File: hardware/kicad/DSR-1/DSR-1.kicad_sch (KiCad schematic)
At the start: 0 parts

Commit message: Refactor code structure for improved readability and maintainability
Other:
- sheet Power input zone ports: added none; removed 9V_PD, B+1_RAW
- sheet Power management ports: added none; removed 9V_PD, B+1_RAW
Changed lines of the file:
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@@
-	(wire
-		(pts
-			(xy 120.65 39.37) (xy 153.67 39.37)
-		)
-		(stroke
-			(width 0)
-			(type default)
-		)
-	)
 	(wire
 		(pts
@@
 	(wire
 		(pts
-			(xy 120.65 43.18) (xy 151.13 43.18)
-		)
-		(stroke
-			(width 0)
-			(type default)
-		)
-	)
-	(wire
-		(pts
-			(xy 153.67 45.72) (xy 163.83 45.72)
-		)
-		(stroke
-			(width 0)
-			(type default)
-		)
-	)
-	(wire
-		(pts
-			(xy 151.13 43.18) (xy 151.13 55.88)
-		)
-		(stroke
-			(width 0)
-			(type default)
-		)
-	)
-	(wire
-		(pts
 			(xy 359.41 22.86) (xy 128.27 22.86)
 		)
@@
 	(wire
 		(pts
-			(xy 151.13 55.88) (xy 163.83 55.88)
-		)
-		(stroke
-			(width 0)
-			(type default)
-		)
-	)
-	(wire
-		(pts
 			(xy 77.47 138.43) (xy 86.36 138.43)
 		)
@@
 		(pts
 			(xy 128.27 22.86) (xy 128.27 54.61)
-		)
-		(stroke
-			(width 0)
-			(type default)
-		)
-	)
-	(wire
-		(pts
-			(xy 153.67 39.37) (xy 153.67 45.72)
 		)
 		(stroke
@@
 			)
 		)
-		(pin "9V_PD" output
-			(at 120.65 39.37 0)
-			(effects
-				(font
-					(size 1.27 1.27)
-				)
-				(justify right)
-			)
-		)
-		(pin "B+1_RAW" output
-			(at 120.65 43.18 0)
-			(effects
-				(font
-					(size 1.27 1.27)
-				)
-				(justify right)
-			)
-		)
 		(pin "CC1" bidirectional
 			(at 120.65 50.8 0)
@@
 			)
 		)
-		(pin "9V_PD" input
-			(at 163.83 45.72 180)
-			(effects
-				(font
-					(size 1.27 1.27)
-				)
-				(justify left)
-			)
-		)
-		(pin "B+1_RAW" input
-			(at 163.83 55.88 180)
-			(effects
-				(font
-					(size 1.27 1.27)
-				)
-				(justify left)
-			)
-		)

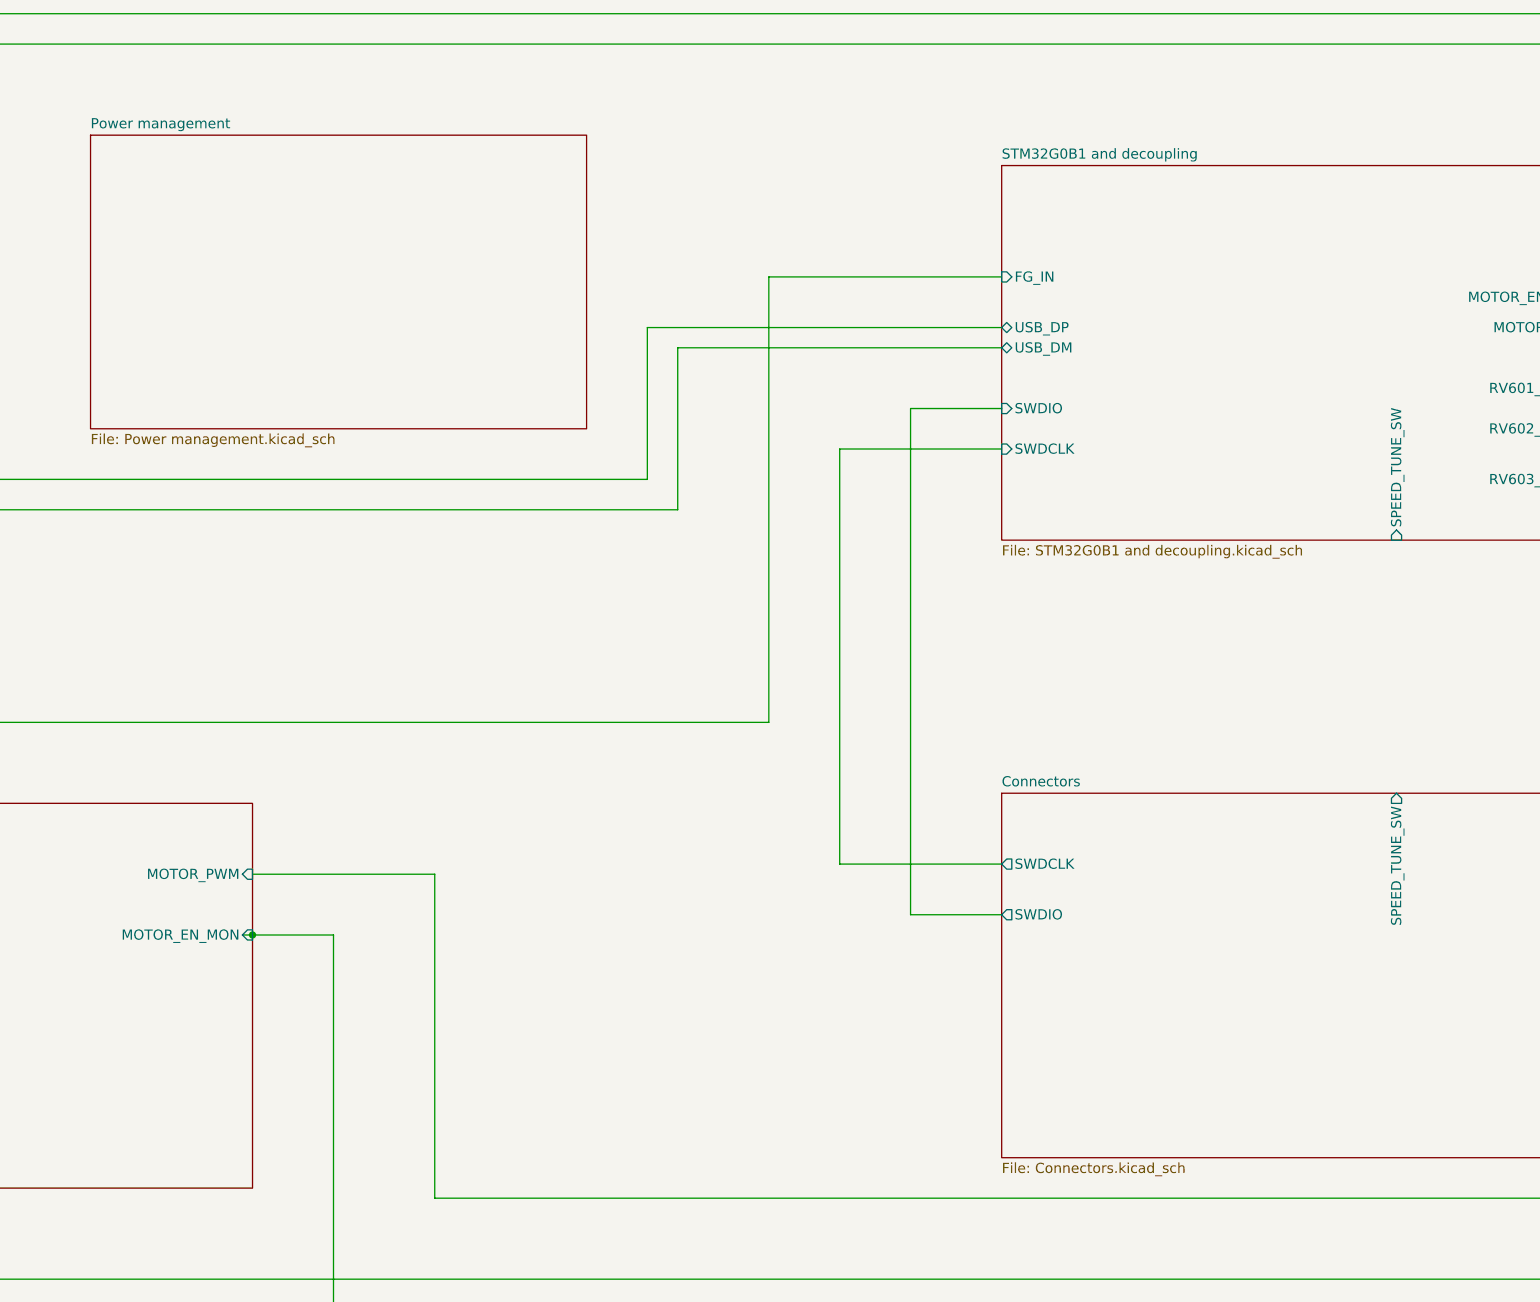
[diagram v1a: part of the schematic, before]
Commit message: completed schematics through sheet 5.
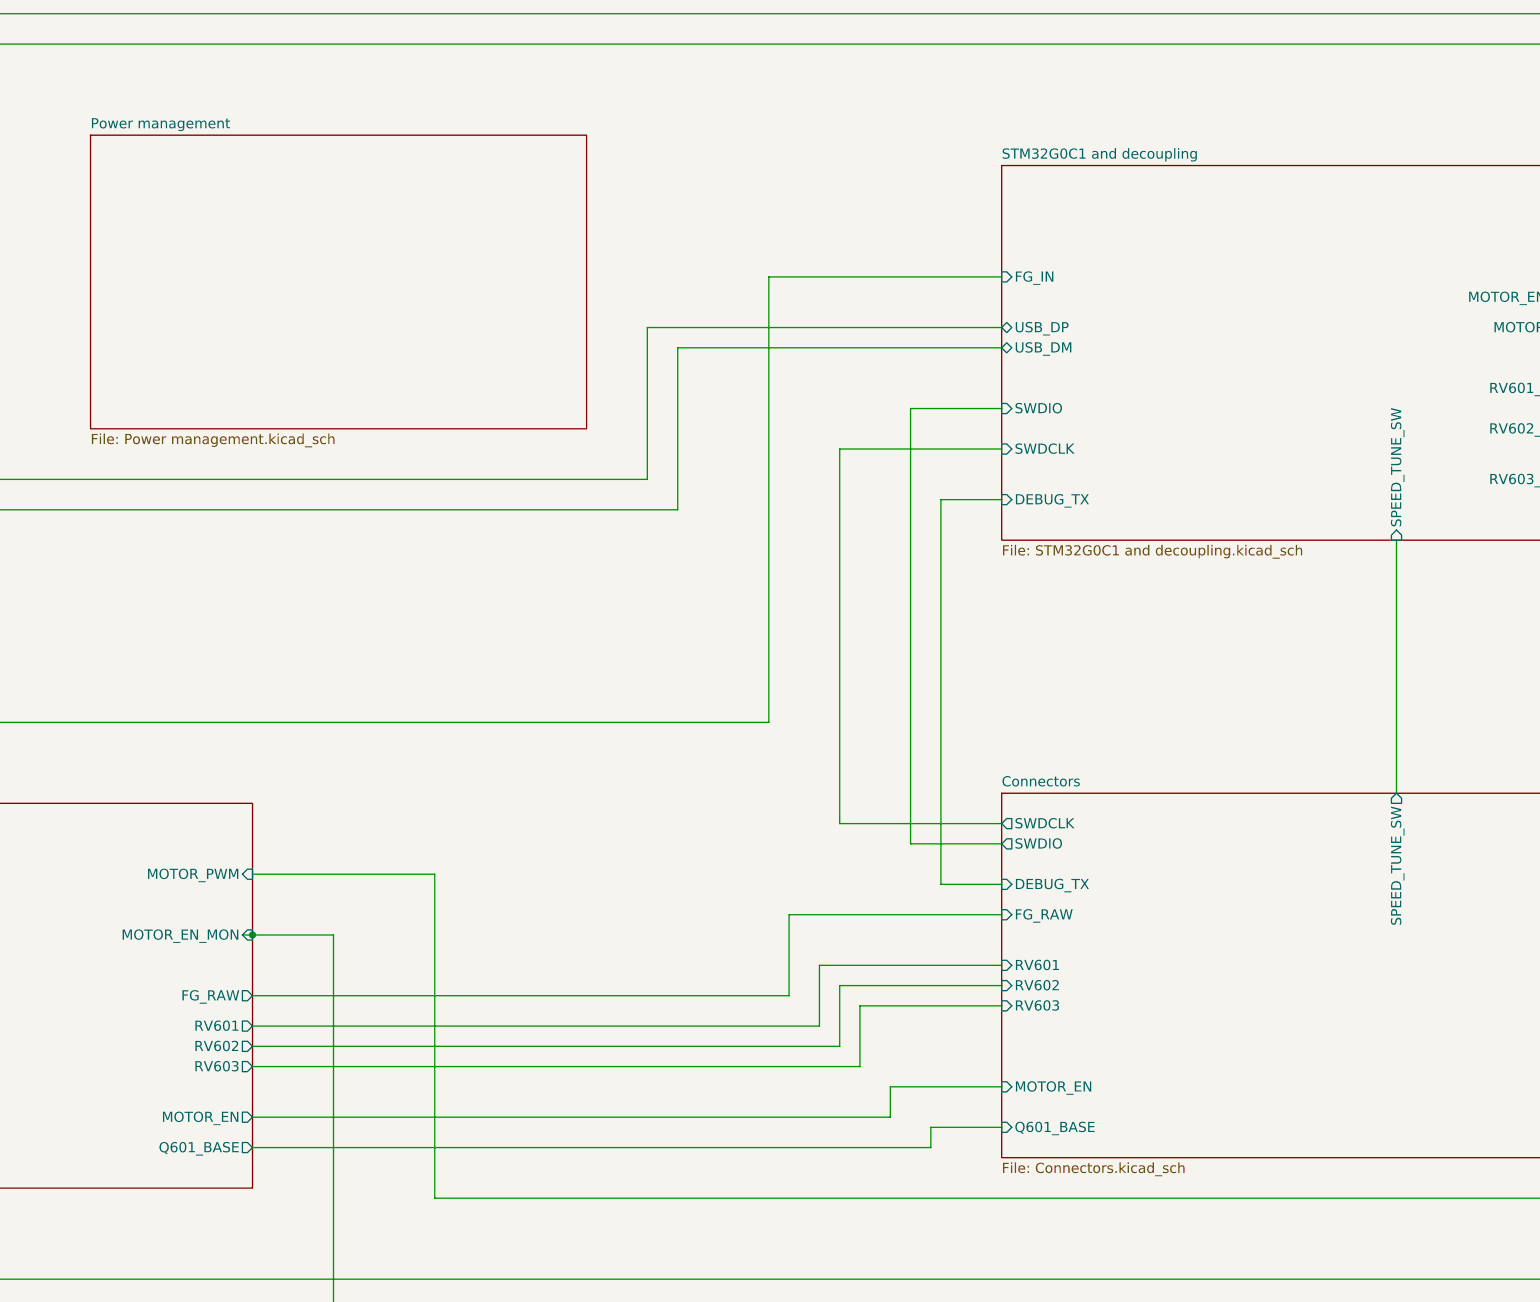
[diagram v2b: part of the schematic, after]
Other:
- sheet STM32G0B1 and decoupling renamed STM32G0C1 and decoupling
- sheet Connectors ports: added DEBUG_TX, FG_RAW, MOTOR_EN, Q601_BASE, RV601, RV602, RV603; removed none
- sheet STM32G0C1 and decoupling: file STM32G0B1 and decoupling.kicad_sch -> STM32G0C1 and decoupling.kicad_sch
- sheet STM32G0C1 and decoupling ports: added DEBUG_TX; removed none
- sheet Signal conditioning ports: added FG_RAW, MOTOR_EN, Q601_BASE, RV601, RV602, RV603; removed none

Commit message: Update position of BRING-UP ORDER text in Power management schematic for better visibility
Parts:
- added C17, C21, C23, C25: 10uf, symbol Device:C_US
- added C18: 100nf, symbol Device:C_US
- added C19: 4.7uf, symbol Device:C_US
- added C20: 22uf, symbol Device:C_US
- added C22: 47uF 16V, symbol Device:C_US
- added C24, C26: 1uF, symbol Device:C_US
- added C27: 100nF, symbol Device:C_US
- added C28: 100nF C0G 10v, symbol Device:C_US
- added C29: 100nF X5R 10v, symbol Device:C_US
- added C30: 1uF 10v, symbol Device:C_US
- added C31: 10pF, symbol Device:C_US
- added C32: 100nF 10V X5R, symbol Device:C_US
- added D12: USBLC6-2SC6Y, USBLC6-2SC6Y:SOT95P280X145-6N, symbol DSR-1:USBLC6-2SC6Y
- added D13, D14, D15, D16, D18: SS14, Diode_SMD:D_SMA, symbol Diode:SS14
- added D17: SMBJ12A-13-F, SMBJ12A-13-F:DIOM5336X250N, symbol SMBJ12A-13-F:SMBJ12A-13-F
- added D19, D20, D21, D22: BAT54S, Package_TO_SOT_SMD:SOT-23, symbol DSR-1:BAT54S
- added F2: Polyfuse, symbol Device:Polyfuse
- added J3: USB_C_Receptacle, symbol DSR-1:USB_C_Receptacle
- added J4: Barrel_Jack, symbol Connector:Barrel_Jack
- added L3: 4.7uH 1.5A, symbol Device:L
- added L4: 4.7uH, symbol Device:L
- added Q2: MMBT3904, Package_TO_SOT_SMD:SOT-23, symbol DSR-1:MMBT3904
- added R16: 100k, symbol Device:R
- added R17: 649k, symbol Device:R
- added R18: 169k, symbol Device:R
- added R19, R20, R21: 10k, symbol Device:R
- added R22: 22k, symbol Device:R
- added R23, R27, R30: 100, symbol Device:R
- added R24: 100k 5%, symbol Device:R
- added R25: 10k 5%, symbol Device:R
- added R26: 1k 5%, symbol Device:R
- added R28: 10k 1%, symbol Device:R
- added R29: 22k 1%, symbol Device:R
- added U10: STM32G0C1KCUx, Package_DFN_QFN:QFN-32-1EP_5x5mm_P0.5mm_EP3.45x3.45mm, symbol MCU_ST_STM32G0:STM32G0C1KCUx
- added U6: AP63203WU-7, AP63203WU-7:SOIC_05WU-7_DIO-M, symbol AP63203WU-7:AP63203WU-7
- added U7: IP2721, IP2721:TSSOP16, symbol DSR-1:IP2721
- added U8: MT3608, Package_TO_SOT_SMD:SOT-23-6, symbol DSR-1:MT3608
- added U9: MCP1700x-330xxTT, Package_TO_SOT_SMD:SOT-23, symbol DSR-1:MCP1700x-330xxTT
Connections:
- net +3.3V: now also C25.1, C28.1, C29.1, C30.1, D12.5 (VBUS), D19.2 (K), D20.2 (K), D21.2 (K), D22.2 (K), U10.4 (VDD), U9.2 (VO)
- net B+1: now also C20.1, C21.1, C23.1, L3.2, R16.1, R17.1, R18.1, R24.2, U8.4 (EN), U8.5 (IN), U9.3 (VI)
- net B+3: now also C22.1, D18.2 (A)
- net GND: now also C17.1, C17.2, C19.1, C19.2, C20.2, C21.2, C22.2, C24.2, C26.2, C27.2, C28.2, C29.2, C30.2, C31.2, C32.2, D12.2 (GND), D14.2 (A), D16.2 (A), D17.1, D17.2, D19.1 (A), D20.1 (A), D21.1 (A), D22.1 (A), F2.2, J3.A1 (GND), J3.A12 (GND), J3.B1 (GND), J3.B12 (GND), J3.SH (SHIELD), Q2.2 (E), R16.2, R19.2, R20.2, R22.1, R29.2, U10.33 (VSS), U10.5 (VSS), U6.2 (EN), U6.3 (VIN), U6.4 (GND), U7.P$11 (SEL), U7.P$16 (VBUS), U7.P$5 (GND), U8.2 (GND), U9.1 (GND)
- new net: C27.1, U10.6 (PF2)
- new net: D13.2 (A), D14.1 (K), J4.2
- new net: Q2.3 (C), R24.1, R25.1
- new net: C18.1, U6.6 (BST)
- new net: C18.2, L3.1, U6.5 (SW)
- new net: C32.1, Q2.1 (B), R26.1
- new net: D13.1 (K), D15.1 (K), F2.1
- new net: D18.1 (K), L4.2
- new net: R17.2, U6.1 (FB)
- new net: D15.2 (A), D16.1 (K), J4.1
- new net: L4.1, U8.1 (SW)
- new net: R18.2, R19.1, U8.3 (FB)
- new net: C25.2, C26.1
- new net: C23.2, C24.1
- new net: J3.A4 (VBUS), J3.A9 (VBUS), J3.B4 (VBUS), J3.B9 (VBUS), U7.P$1 (VBUSG), U7.P$2 (VIN)
- new net: D12.3 (I/O2_1), J3.A6 (D+), J3.B6 (D+)
- new net: D12.1 (I/O1_1), J3.A7 (D-), J3.B7 (D-)
- new net CC1: J3.A5 (CC1), U10.18 (PA8), U7.P$13 (CC1)
- new net CC2: J3.B5 (CC2), U10.19 (PA9/UCPD1_DBCC1), U7.P$12 (CC2)
- new net DEBUG_TX: U10.30 (PB6)
- new net FG_IN: C31.1, D19.3 (COM), R21.2, R22.2, U10.7 (PA0)
- new net FG_RAW: R21.1
- new net MOTOR_EN: R28.1
- new net MOTOR_EN_MON: R28.2, R29.1, U10.12 (PA5)
- new net MOTOR_PWM: R26.2, U10.13 (PA6)
- new net Q601_BASE: R25.2
- new net RV601: R23.1
- new net RV601_WIPER: D20.3 (COM), R23.2, U10.8 (PA1)
- new net RV602: R27.1
- new net RV602_WIPER: D21.3 (COM), R27.2, U10.9 (PA2)
- new net RV603: R30.1
- new net RV603_WIPER: D22.3 (COM), R30.2, U10.10 (PA3)
- new net SPEED_TUNE_SW: U10.14 (PA7)
- new net SWDCLK: R20.1, U10.25 (PA14)
- new net SWDIO: U10.24 (PA13)
- new net USB_DM: D12.6 (I/O1_2), U10.22 (PA9/PA11)
- new net USB_DP: D12.4 (I/O2_2), U10.23 (PA10/PA12)
- no-connect marks 0 -> 15
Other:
- removed sheet Connectors
- removed sheet Power input zone
- removed sheet Power management
- removed sheet STM32G0C1 and decoupling
- removed sheet Signal conditioning
- note added: "+"
- note added: "10v"
- note added: "16v"
- note added: "ADC Inputs - RV601, RV602, RV603 (J1 Pins 4, 5, 6 → PA1, PA2, PA3)"
- note added: "B+1 output = 0.8 × (1 + 649k/100k) = 6.19V EN tied to VIN - AP63203 internal clamp handles 9V input safely. C3 (BST cap) must be placed within 1mm of BST/SW pins on PCB."
- note added: "B+3 output = 0.6 × (1 + 169k/10k) = 10.74V nominal. ⚠ SW NODE: high dV/dt at 1.2MHz. Keep SW trace <3mm. Minimum 2mm clearance to FG, ADC, and motor drive signal traces. C8 must be 47µF (not 22µF) - X5R derating at 10.8V reduces effective capacitance. Use 16V rated part for adequate margin."
- note added: "BRING-UP ORDER: 1. Verify 9V_PD present before AP63203 powers up 2. Check B+1 = 6.0-6.2V before enabling downstream 3. Check B+3 = 10.5-11V (no load) 4. Check +3.3V = 3.3V ±2% 5. Do not connect WM-D6C harness until all rails verified"
- note added: "C11 (C0G) must be placed closest to pin 4 on PCB. C0G for ADC noise - do not substitute X5R here. EP (pin 33): via array 2×2 or 3×3 grid, 0.3mm drill."
- note added: "CC1 (PA8) and CC2 (PA9) connect to both IP2721 (PD negotiation) and STM32 UCPD1 (monitoring/control). Firmware must clear SYSCFG_CFGR1 UCPD_STROBE early in startup - see RM0444 §28 for UCPD init sequence."
- note added: "FG Signal Path (J1 Pin 1 → PA0)"
- note added: "Fixed 3.3V LDO. VIN max 16V - B+1 = 6V nominal, margin adequate. Requires minimum 1µF on VOUT for stability - C7+C10 exceed this."
- note added: "MOTOR_EN tap point: IC601 footprint pin 7 pad on WM-D6C main board. Verify voltage on bench before connecting. See signal-chain-analysis.md §3."
- note added: "Motor Drive Output (PA6 → J1 Pin 2 → Q601 base)"
- note added: "Motor Enable Monitor (J1 Pin 3 → PA5)"
- note added: "PA9/PA10 can remap to PA11/PA12 pins via SYSCFG_CFGR1. Do not remap while USB is active. PCB: route as 90Ω differential pair, matched length, ≤25mm, away from MT3608 SW node."
- note added: "Q601 (2SB1013 PNP) is on WM-D6C main board - NOT on DSR-1 PCB. Q601 emitter → B+3 via Q703/Q704 mode-switch chain. Q601 base operating range must be measured on bench to confirm R9 sizing. See signal-chain-analysis.md §2."
- note added: "R5 holds BOOT0 low at reset → normal boot from flash. To enter system bootloader: pull PA14 high before reset via SWD header. Do not remove R5 - floating BOOT0 causes unpredictable boot behavior."
- note added: "RV601"
- note added: "RV602"
- note added: "RV603"
- note added: "SEL pin sets PD voltage request - verify correct resistor value against IP2721 datasheet for 9V profile before ordering PCB. VBUSG must be tied to VIN. Floating VBUSG prevents output enable after negotiation regardless of CC state."
- note added: "VERIFY ACTUAL FG SWING ON BENCH BEFORE POWER-ON. R4 value may need adjustment based on measured B+1 and pull-up resistor. See signal-chain-analysis.md §1 for formula. Do not connect FG directly to PA0 without confirming the conditioned voltage is below 3.3V."
- note added: "VERIFY WIPER VOLTAGE BEFORE POWER-ON. See signal-chain- analysis.md §4 for divider formula. If wiper exceeds 3.3V, add R/2R divider before the 100Ω series resistor. Adjust ADC scaling in firmware to match."
- note added: "VERIFY WIPER VOLTAGES ON BENCH BEFORE POWER-ON. If any wiper exceeds 3.3V at B+1 = 6V, add resistor divider on Sheet 5 before the clamp diodes. See signal-chain-analysis.md §4."
- note added: "Variant A - USB-C PD/Data"
- note added: "Variant B - Barrel Jack, Polarity Agnostic"
- note added: "Variant B input: 9V DC nominal, 5.5mm/2.1mm barrel jack. Polarity agnostic - bridge rectifier output is always positive. Do NOT connect a 6V adapter - minimum 7.5V required after 0.8V bridge drop to maintain regulation headroom. SMBJ12A: standoff 12V, clamp 19.9V max. AP63203 VIN abs max 32V."
